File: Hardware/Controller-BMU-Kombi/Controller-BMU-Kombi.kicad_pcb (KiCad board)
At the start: 2 copper layers, 15 parts, among them J1 Conn_01x05_Socket, J2 Conn_01x05_Socket, J3 Conn_01x05_Socket, J4 Conn_01x05_Socket

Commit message: Updates
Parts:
- added J5: Conn_01x05_Socket, Connector_PinSocket_2.54mm:PinSocket_1x05_P2.54mm_Horizontal, F.Cu at (182.6, 116.6)
- added J6: Conn_01x05_Socket, Connector_PinSocket_2.54mm:PinSocket_1x05_P2.54mm_Horizontal, F.Cu at (196.0, 116.6)
- added U2: ~, Batteriestecker:Batteriestecker, F.Cu at (154.0, 147.5)
- A1: value 113990105 -> Arduino_UNO_R2; footprint 113990105:SEEED_113990105 -> Module:Arduino_UNO_R2
- moved A1 60.5 mm to (69.0, 146.6), turned to 90 degrees

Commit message: updated
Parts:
- removed U2: ~, Batteriestecker:Batteriestecker
- added BT2: BK-18650-PC8, BK-18650-PC8:BAT_BK-18650-PC8, B.Cu at (197.5, 63.0)
- moved U1 32.5 mm to (123.0, 109.0)
- moved A1 14.3 mm to (55.2, 150.6)
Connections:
- net Net-(J1-Pin_4) renamed CELLS+
- net Net-(J4-Pin_5) renamed CELLS-

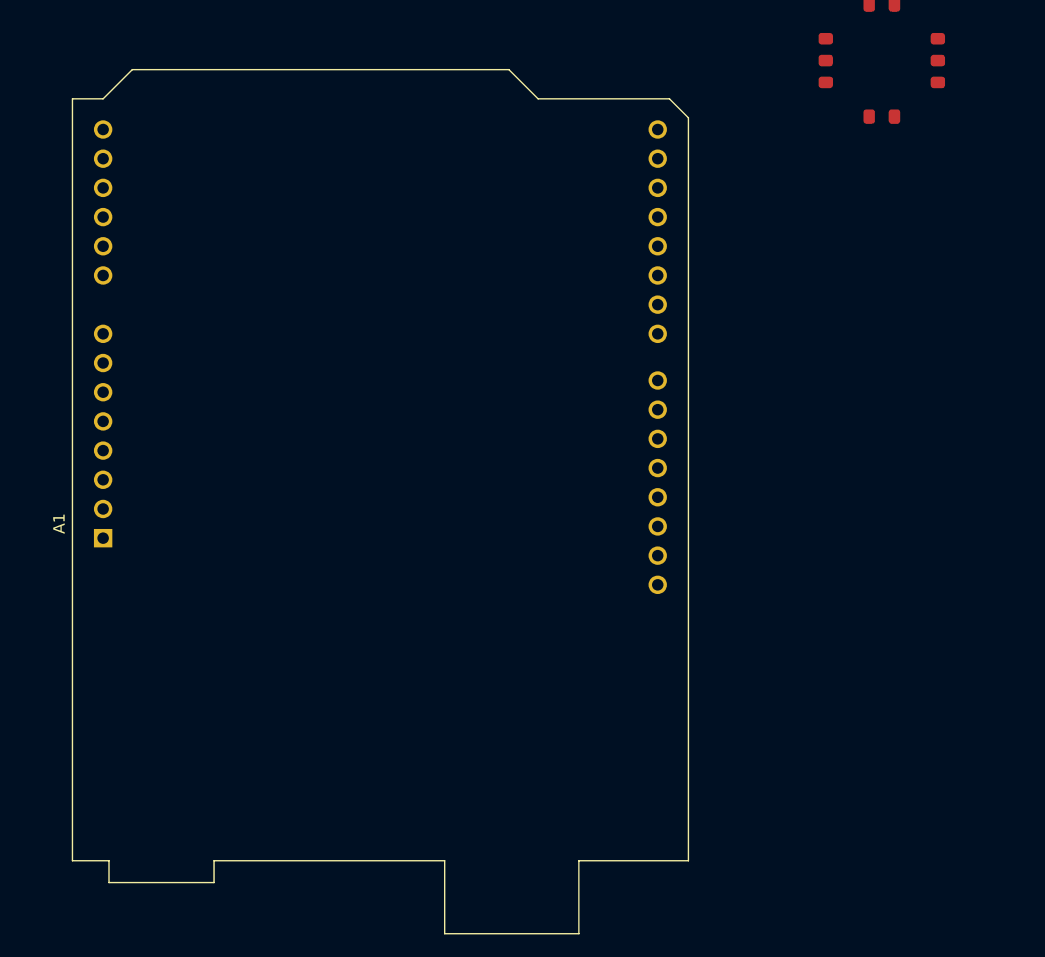
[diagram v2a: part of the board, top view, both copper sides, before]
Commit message: added circuitry for user controls
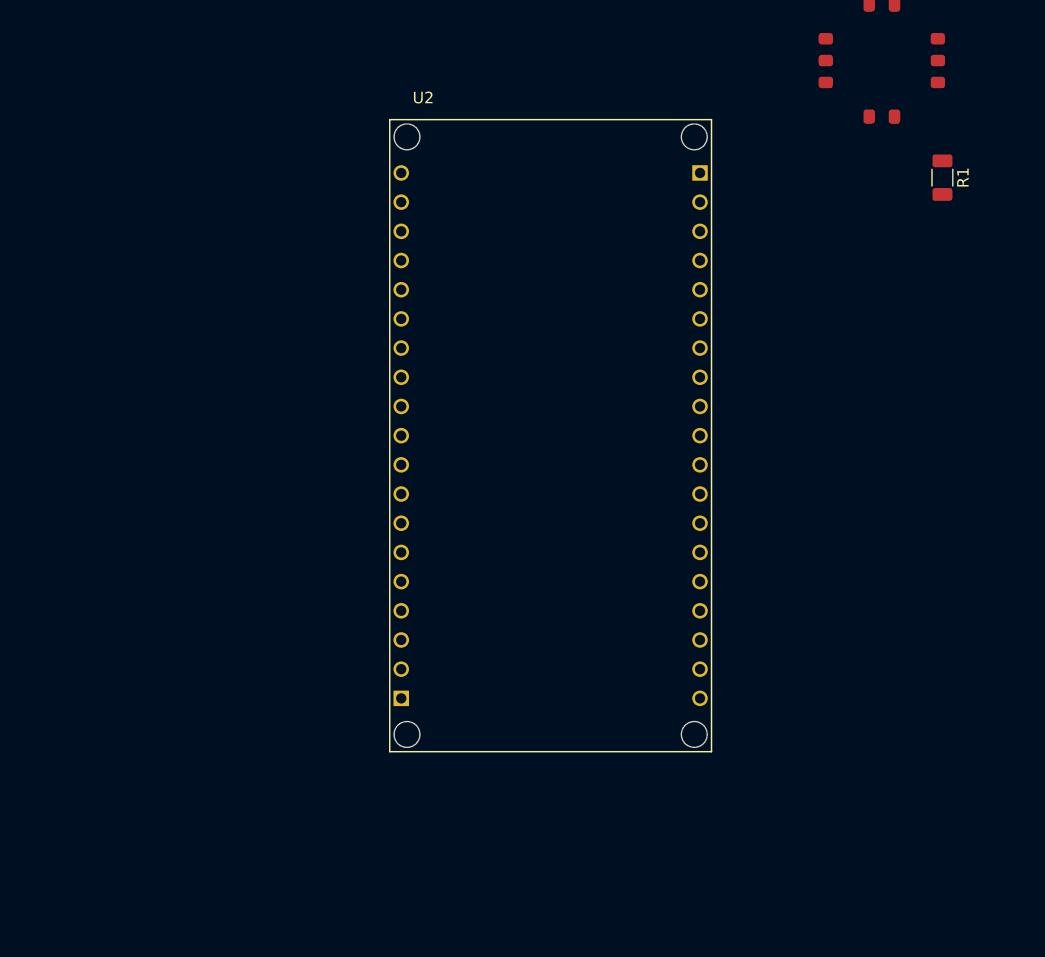
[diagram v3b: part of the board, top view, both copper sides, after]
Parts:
- removed A1: Arduino_UNO_R2, Module:Arduino_UNO_R2
- added R1: 10k, Resistor_SMD:R_1206_3216Metric, F.Cu at (128.3, 119.2)
- added U2: ESP32_NODEMCU, ESP32_NODEMCU:MODULE_ESP32_NODEMCU, F.Cu at (94.2, 141.6)
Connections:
- J6 pad 5: SW1 -> SW2
- U1 pad 1: unconnected-(U1-Pad1) -> BUT1
- U1 pad 10: unconnected-(U1-Pad10) -> Net-(R1-Pad1)
- U1 pad 2: unconnected-(U1-Pad2) -> BUT2
- U1 pad 3: unconnected-(U1-Pad3) -> Net-(R1-Pad1)
- U1 pad 4: unconnected-(U1-Pad4) -> BUT3
- U1 pad 5: unconnected-(U1-Pad5) -> BUT4
- U1 pad 6: unconnected-(U1-Pad6) -> Net-(R1-Pad1)
- U1 pad 7: unconnected-(U1-Pad7) -> BUT5
- U1 pad 8: unconnected-(U1-Pad8) -> Net-(R1-Pad1)
- U1 pad 9: unconnected-(U1-Pad9) -> Net-(R1-Pad1)

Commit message: synchronizing
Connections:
- net CELLS+ renamed CELL1+
- net Net-(BT2-Pad1-) renamed CELL2+
- net Net-(BT2-Pad2-) renamed CELL3+
- net Net-(BT2-Pad3-) renamed CELL4+
- BT2 pad 4-: CELLS- -> BAT-
- J4 pad 5: CELLS- -> Net-(J4-Pin_5)
- TP8 pad 1: CELLS- -> Net-(J4-Pin_5)
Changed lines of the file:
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@@
 	(net 29 "+5V")
 	(net 30 "GND")
-	(net 31 "CELLS-")
-	(net 32 "Net-(BT2-Pad1-)")
-	(net 33 "Net-(BT2-Pad2-)")
-	(net 34 "Net-(BT2-Pad3-)")
-	(net 35 "CELLS+")
+	(net 31 "BAT-")
+	(net 32 "CELL2+")
+	(net 33 "CELL3+")
+	(net 34 "CELL4+")
+	(net 35 "CELL1+")
 	(net 36 "unconnected-(U2-G16-PadJ4_12)")
 	(net 37 "unconnected-(U2-CLK-PadJ4_19)")
@@
 	(net 52 "BUT4")
 	(net 53 "BUT2")
+	(net 54 "Net-(J4-Pin_5)")
 	(footprint "Connector_PinSocket_2.54mm:PinSocket_1x05_P2.54mm_Horizontal"
 		(layer "F.Cu")
@@
 			(layers "*.Cu" "*.Mask")
 			(remove_unused_layers no)
-			(net 35 "CELLS+")
+			(net 35 "CELL1+")
 			(pinfunction "Pin_4")
 			(pintype "passive")
@@
 			(layers "*.Cu" "*.Mask")
 			(remove_unused_layers no)
-			(net 35 "CELLS+")
+			(net 35 "CELL1+")
 			(pinfunction "1")
 			(pintype "passive")
@@
 			(layers "*.Cu" "*.Mask")
 			(remove_unused_layers no)
-			(net 31 "CELLS-")
+			(net 54 "Net-(J4-Pin_5)")
 			(pinfunction "1")
 			(pintype "passive")
@@
 			(layers "*.Cu" "*.Mask")
 			(remove_unused_layers no)
-			(net 31 "CELLS-")
+			(net 54 "Net-(J4-Pin_5)")
 			(pinfunction "Pin_5")
 			(pintype "passive")
@@
 			(layers "*.Cu" "*.Mask")
 			(remove_unused_layers no)
-			(net 35 "CELLS+")
+			(net 35 "CELL1+")
 			(pintype "passive")
 			(solder_mask_margin 0.102)
@@
 			(layers "*.Cu" "*.Mask")
 			(remove_unused_layers no)
-			(net 32 "Net-(BT2-Pad1-)")
+			(net 32 "CELL2+")
 			(pintype "passive")
 			(solder_mask_margin 0.102)
@@
 			(layers "*.Cu" "*.Mask")
 			(remove_unused_layers no)
-			(net 32 "Net-(BT2-Pad1-)")
+			(net 32 "CELL2+")
 			(pintype "passive")
 			(solder_mask_margin 0.102)
@@
 			(layers "*.Cu" "*.Mask")
 			(remove_unused_layers no)
-			(net 33 "Net-(BT2-Pad2-)")
+			(net 33 "CELL3+")
 			(pintype "passive")
 			(solder_mask_margin 0.102)
@@
 			(layers "*.Cu" "*.Mask")
 			(remove_unused_layers no)
-			(net 33 "Net-(BT2-Pad2-)")
+			(net 33 "CELL3+")
 			(pintype "passive")
 			(solder_mask_margin 0.102)
@@
 			(layers "*.Cu" "*.Mask")
 			(remove_unused_layers no)
-			(net 34 "Net-(BT2-Pad3-)")
+			(net 34 "CELL4+")
 			(pintype "passive")
 			(solder_mask_margin 0.102)
@@
 			(layers "*.Cu" "*.Mask")
 			(remove_unused_layers no)
-			(net 34 "Net-(BT2-Pad3-)")
+			(net 34 "CELL4+")
 			(pintype "passive")
 			(solder_mask_margin 0.102)
@@
 			(layers "*.Cu" "*.Mask")
 			(remove_unused_layers no)
-			(net 31 "CELLS-")
+			(net 31 "BAT-")
 			(pintype "passive")
 			(solder_mask_margin 0.102)
